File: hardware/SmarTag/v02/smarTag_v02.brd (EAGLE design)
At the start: 31.8 x 24.1 mm, 17 parts, among them U1 ADXL362

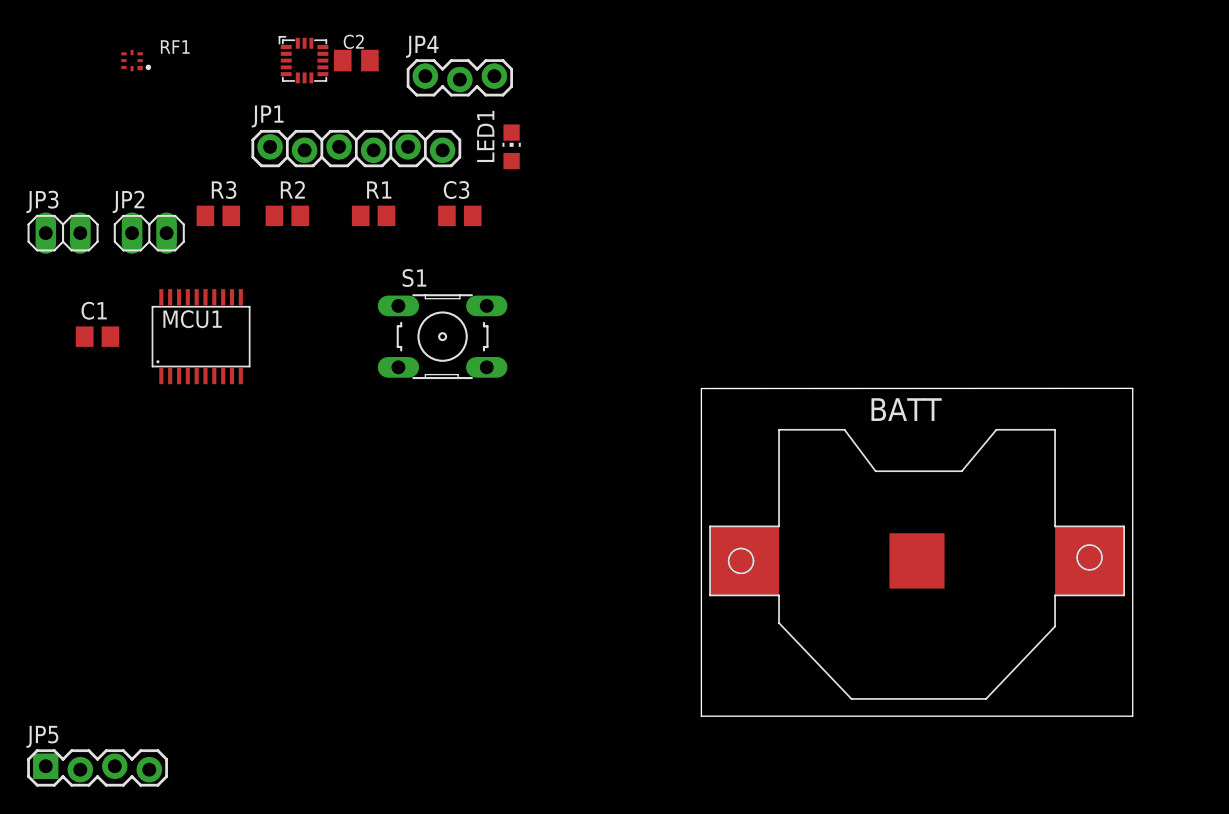
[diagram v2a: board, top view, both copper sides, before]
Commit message: hw: Add v02 board.
A complete rework of the board. Includes a new SMD hard switch, no extraneous breakout board headers, and a much smaller overall profile.
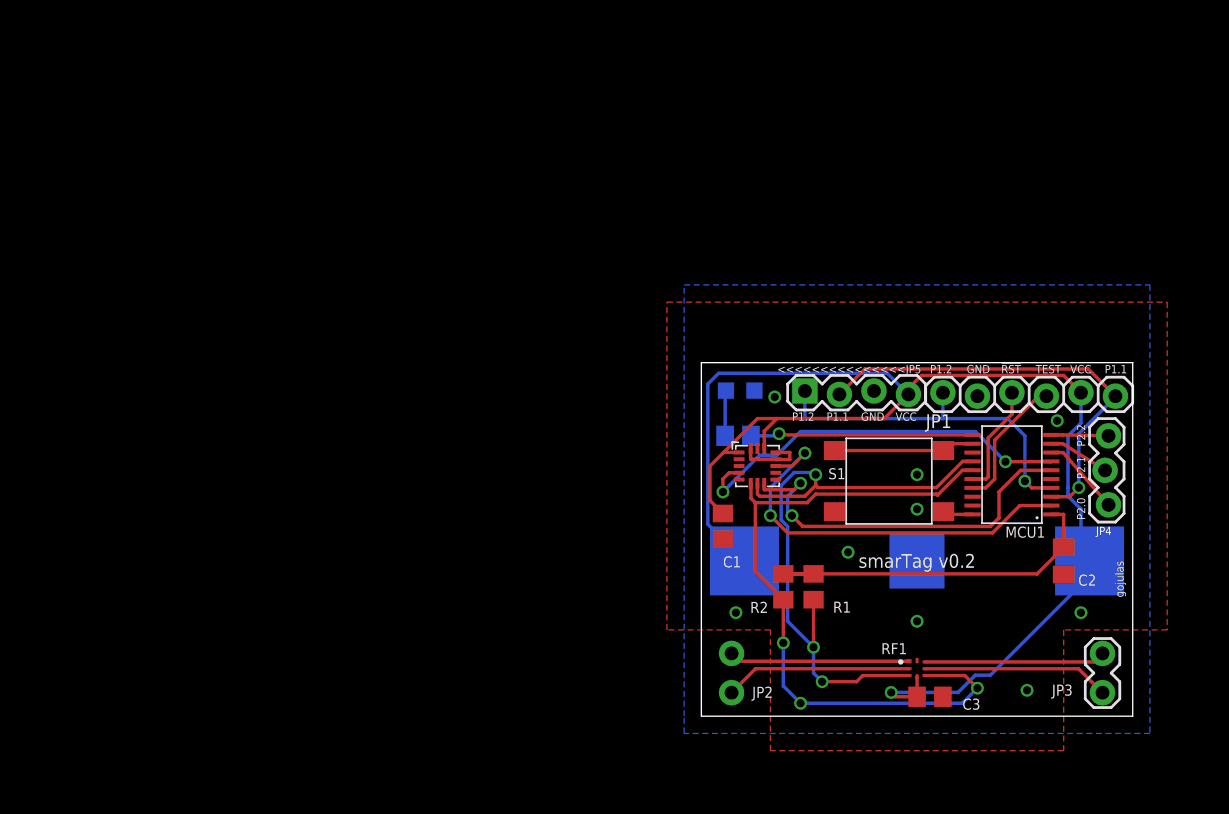
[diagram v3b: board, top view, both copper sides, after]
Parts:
- JP2, JP3: device pinhead:1X02 -> SparkFun-Connectors:1X02_LOCK
- S1: device switch-omron:B3F-10XX -> PP_Electromechanical:B3FS-1000
- moved JP3 83.6 mm to (29.5, 1.91), turned to 90 degrees
- moved RF1 73.1 mm to (15.9, 3.49), turned to 180 degrees
- moved C2 63.8 mm to (26.7, 11.4), turned to 270 degrees
- moved JP5 62.3 mm to (7.62, 23.8)
- moved MCU1 60.5 mm to (22.9, 17.8), turned to 90 degrees
- moved JP4 56.7 mm to (29.8, 20.6), turned to 270 degrees
- moved JP2 54.5 mm to (2.22, 1.91), flipped to the bottom, turned to 90 degrees
- moved JP1 52.7 mm to (17.8, 23.8)
- moved C3 49.5 mm to (16.8, 1.43)
- moved C1 48.1 mm to (1.59, 14.0), turned to 270 degrees
- moved R2 45.6 mm to (6.03, 9.53), turned to 270 degrees
- moved U1 44.7 mm to (4.13, 18.4)
- moved R1 42.4 mm to (8.26, 9.53), turned to 270 degrees
- moved R3 41.5 mm to (2.70, 20.6), flipped to the bottom
- moved S1 34.5 mm to (13.8, 17.3), turned to 180 degrees
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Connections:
- net GND: now also S1.3, S1.4; no longer S1.1, S1.2
- net P2.4: now also S1.1, S1.2; no longer S1.3, S1.4
- net RF1N: now also JP2.1; no longer JP2.2
- net RF1P: now also JP2.2; no longer JP2.1
- net RF2N: now also JP3.1; no longer JP3.2
- net RF2P: now also JP3.2; no longer JP3.1
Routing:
- net VCC: track 0.00 -> 135.9 mm, vias 0 -> 1
- net P1.7: track 0.00 -> 52.5 mm, vias 0 -> 3
- net P1.6: track 0.00 -> 47.4 mm, vias 0 -> 3
- net P1.1/RX: track 0.00 -> 32.1 mm, vias 0 -> 1
- net P1.0: track 0.00 -> 30.2 mm, vias 0 -> 2
- net P1.5: track 0.00 -> 29.3 mm, vias 0 -> 2
- net P1.4: track 0.00 -> 28.5 mm, vias 0 -> 2
- net P1.2/TX: track 0.00 -> 26.1 mm, vias 0 -> 1
- net P2.3: track 0.00 -> 16.4 mm, vias 0 -> 1
- net RF1N: track 0.00 -> 14.5 mm
- net RF2N: track 0.00 -> 13.8 mm
- net RF2P: track 0.00 -> 13.3 mm
- net RF1P: track 0.00 -> 13.3 mm
- net P2.4: track 0.00 -> 10.4 mm
- net TEST: track 0.00 -> 9.91 mm
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- added copper zone on layer 1, net GND
- added copper zone on layer 16, net GND
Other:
- board size 31.8 x 24.1 mm -> 31.8 x 26 mm
- board text added: "!RST"
- board text added: "<<<<<<<<<<<<<<<<<<<<<<"
- board text added: "<<<<<<<<<<<<<<<JP5"
- board text added: ">>>>>>>>>>>>>>>"
- board text added: "GND"
- board text added: "JP1"
- board text added: "JP4"
- board text added: "JP5>>>>>>>>>>>>>>>"
- board text added: "P1.1"
- board text added: "P1.2"
- board text added: "P2.0"
- board text added: "P2.1"
- board text added: "P2.2"
- board text added: "TEST"
- board text added: "VCC"
- board text added: "gojulas"
- board text added: "smarTag v0.2"

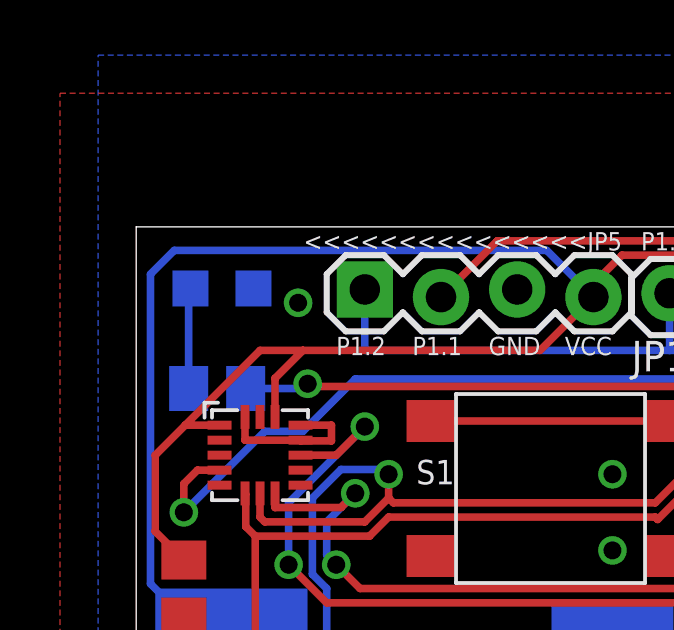
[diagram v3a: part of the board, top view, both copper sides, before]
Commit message: hw: Move Status LED topside
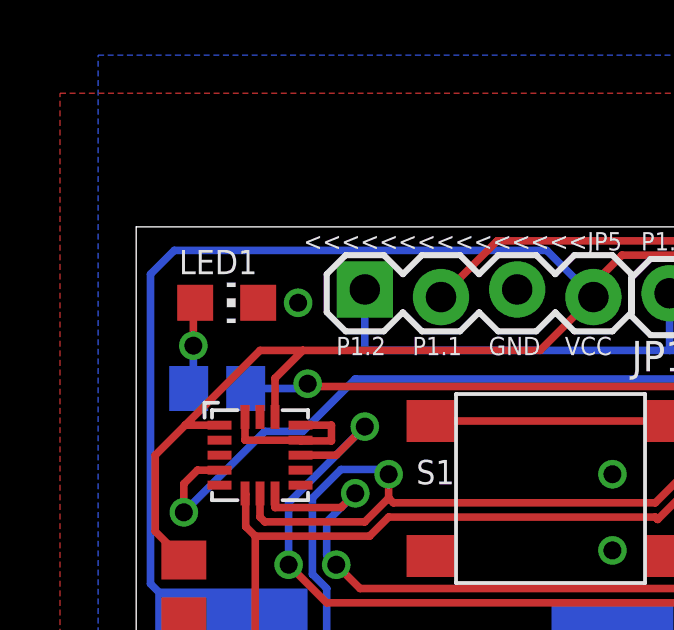
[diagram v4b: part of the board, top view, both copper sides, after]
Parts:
- moved LED1 0.50 mm to (3.02, 23.5), flipped to the top, turned to 270 degrees
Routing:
- net N$1: track 3.36 -> 3.08 mm, vias 0 -> 1
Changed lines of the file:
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@@
 <attribute name="VALUE" x="26.67" y="21.9075" size="1.27" layer="27" rot="R270"/>
 </element>
-<element name="LED1" library="led" package="CHIP-LED0805" value="" x="2.8575" y="23.97125" smashed="yes" rot="MR90">
-<attribute name="NAME" x="1.27" y="23.01875" size="0.8128" layer="26" font="vector" ratio="12" rot="MR180"/>
-<attribute name="VALUE" x="1.5875" y="26.51125" size="1.27" layer="28" rot="MR180"/>
+<element name="LED1" library="led" package="CHIP-LED0805" value="" x="3.01625" y="23.495" smashed="yes" rot="R270">
+<attribute name="NAME" x="1.42875" y="24.4475" size="0.8128" layer="25" font="vector" ratio="12"/>
+<attribute name="VALUE" x="1.74625" y="20.955" size="1.27" layer="27"/>
 </element>
 <element name="MCU1" library="TI_MSP430_v16" package="PW20" value="G2X[1/5]2---PW20" x="22.86" y="17.78" smashed="yes" rot="R90">
@@
 <contactref element="R3" pad="2"/>
 <contactref element="LED1" pad="A"/>
-<wire x1="1.74875" y1="20.6375" x2="1.74875" y2="23.9125" width="0.254" layer="16"/>
-<wire x1="1.74875" y1="23.9125" x2="1.8075" y2="23.97125" width="0.254" layer="16"/>
+<wire x1="1.74875" y1="20.6375" x2="1.905" y2="20.6375" width="0.254" layer="16"/>
+<wire x1="1.905" y1="20.6375" x2="1.905" y2="22.06625" width="0.254" layer="16"/>
+<via x="1.905" y="22.06625" extent="1-16" drill="0.6"/>
+<wire x1="1.905" y1="22.06625" x2="1.905" y2="23.495" width="0.254" layer="1"/>
+<wire x1="1.905" y1="23.495" x2="1.96625" y2="23.495" width="0.254" layer="1"/>
 </signal>
 <signal name="P2.3">

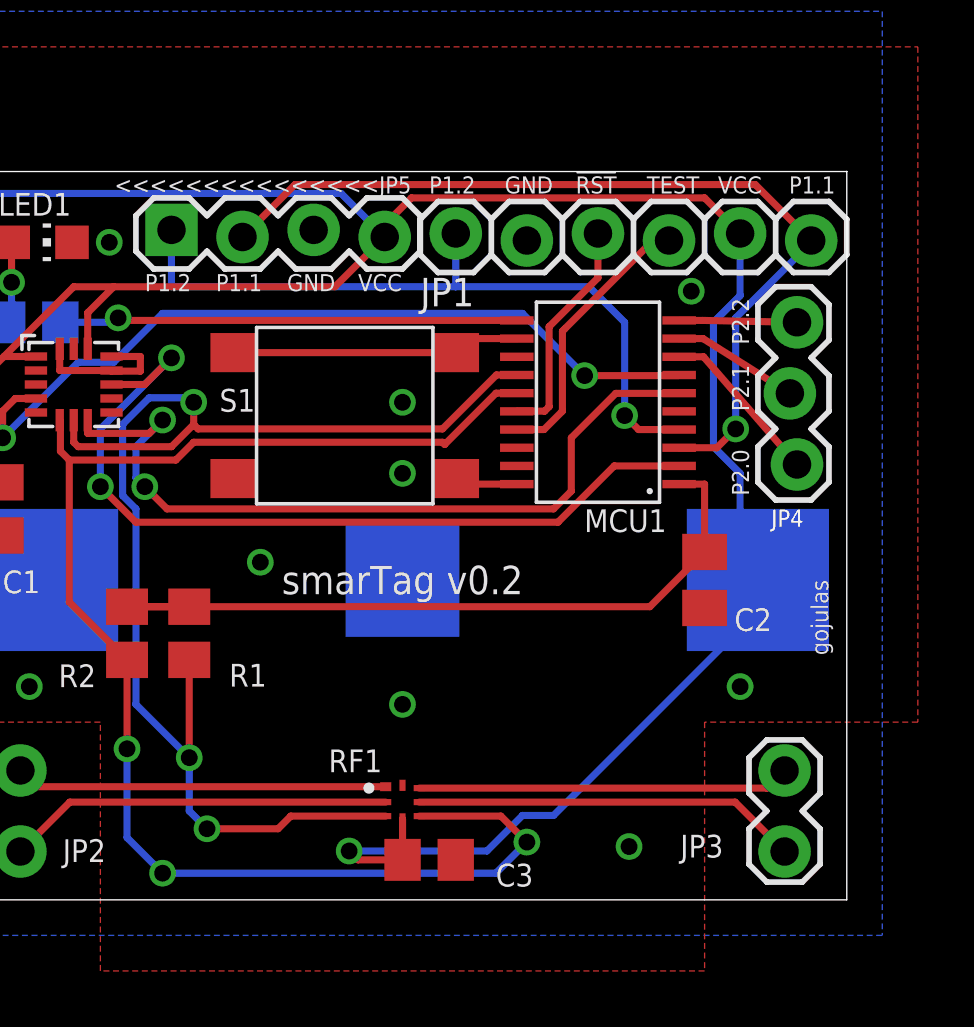
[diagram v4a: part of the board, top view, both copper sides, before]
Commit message: hw: Update board w/ 1.27mm JP1
This new programming header allows for direct connection with an MSP430
Launchpad for programming and debugging.
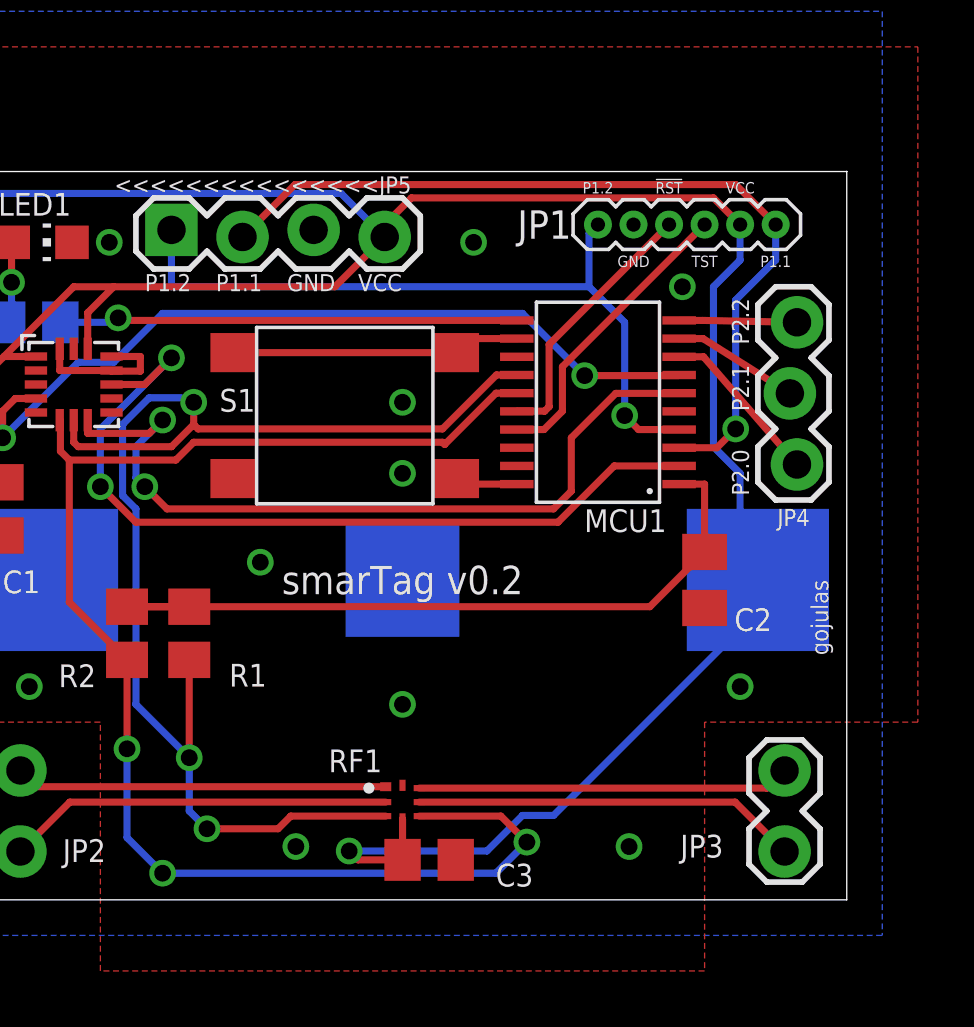
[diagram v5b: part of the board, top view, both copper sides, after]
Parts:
- JP1: device SparkFun-Connectors:1X06_LOCK -> SparkFun-Connectors:1X06-1.27MM
- moved JP1 5.09 mm to (22.9, 24.1)
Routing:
- net P1.1/RX: track 32.1 -> 30.6 mm
- net !RST: track 8.14 -> 9.51 mm
- net TEST: track 9.91 -> 10.7 mm
- net GND: vias 9 -> 11
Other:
- board text added: "TST"
- board text removed: "<<<<<<<<<<<<<<<<<<<<<<"
- board text removed: ">>>>>>>>>>>>>>>"

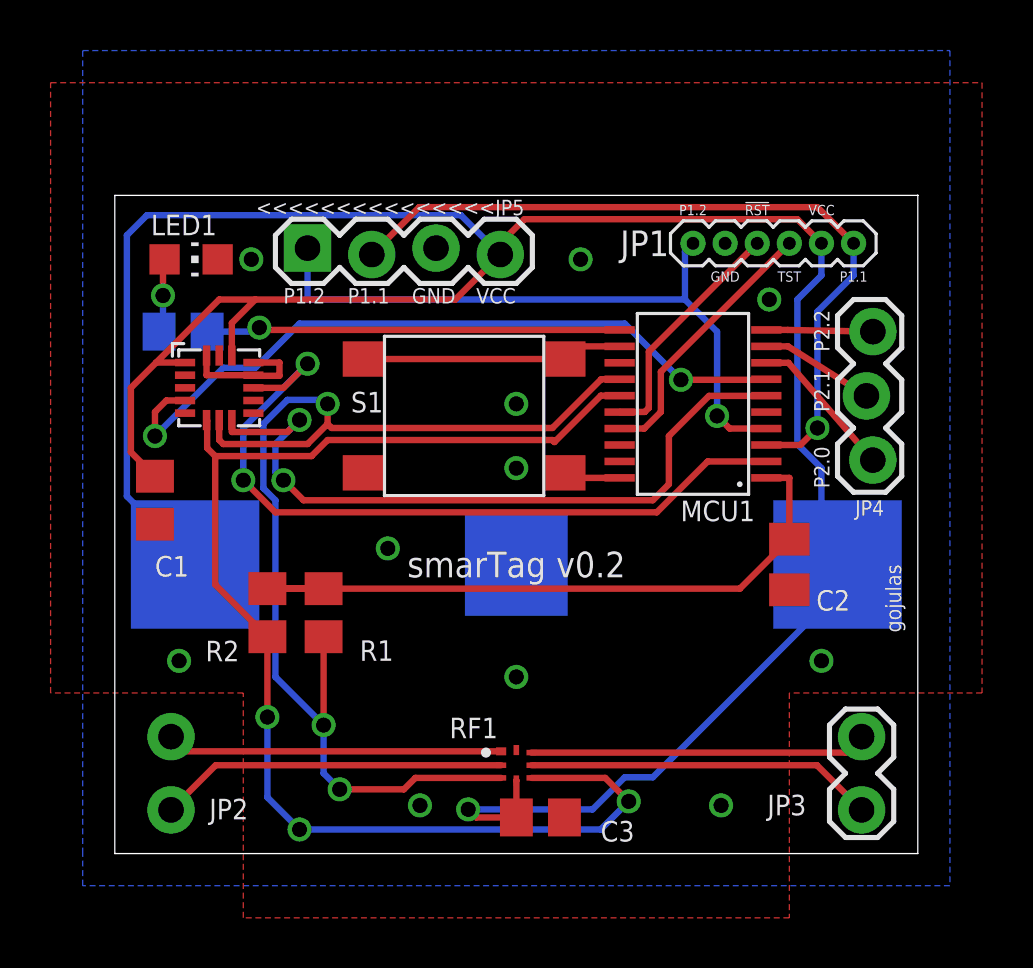
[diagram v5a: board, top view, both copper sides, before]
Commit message: hw: Add final touches for first production run.
Add tenting to vias.
Adjust vias away from battery pads.
Passed EDC and DRC.

This version sent to Oshpark on 04-19-2016
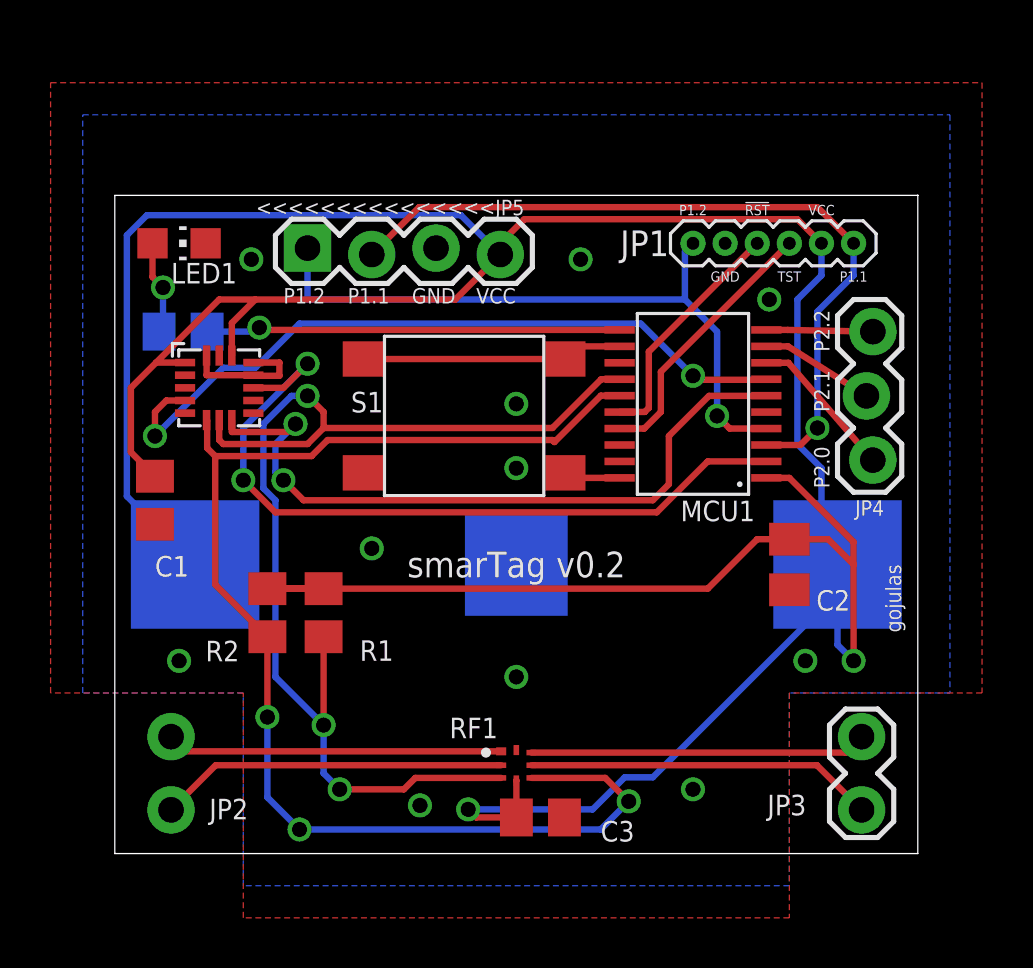
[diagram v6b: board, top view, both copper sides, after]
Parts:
- moved LED1 0.79 mm to (2.54, 24.1)
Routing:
- net VCC: track 136.1 -> 146.6 mm, vias 1 -> 2
- net N$1: track 3.08 -> 3.82 mm
